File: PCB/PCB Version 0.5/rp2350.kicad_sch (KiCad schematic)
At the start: 27 parts, among them U1 RP2350A, U10 W25Q16JVUXIQ, Y1 Crystal_GND24

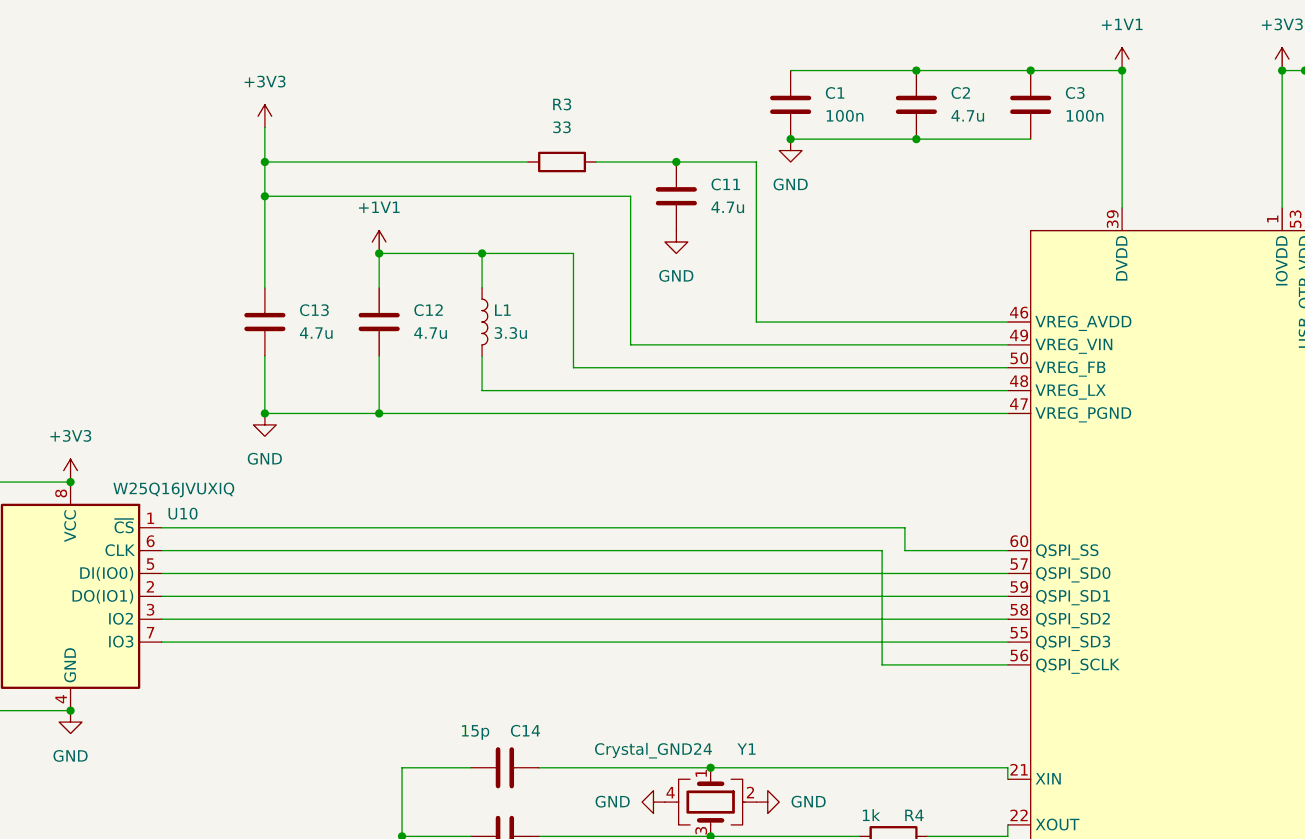
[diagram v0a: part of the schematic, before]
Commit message: add BOM
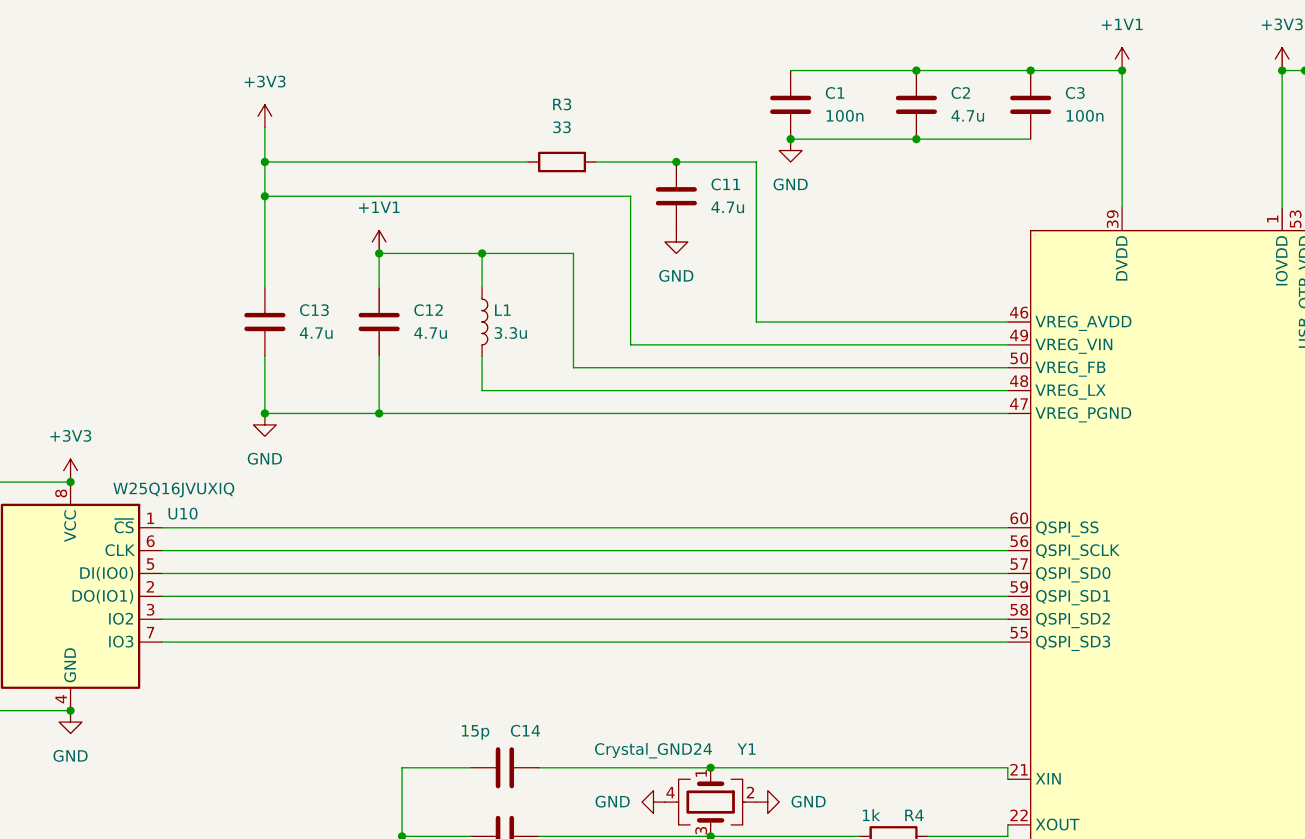
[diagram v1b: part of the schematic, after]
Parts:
- C11, C12, C13: footprint (none) -> Capacitor_SMD:C_0402_1005Metric
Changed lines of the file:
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@@
 	)
 	(junction
-		(at 100.33 92.71)
-		(diameter 0)
-		(color 0 0 0 0)
-	)
-	(junction
 		(at 278.13 82.55)
 		(diameter 0)
@@
 	)
 	(junction
+		(at 100.33 92.71)
+		(diameter 0)
+		(color 0 0 0 0)
+	)
+	(junction
 		(at 100.33 96.52)
 		(diameter 0)
@@
 	(wire
 		(pts
-			(xy 100.33 96.52) (xy 100.33 92.71)
-		)
-		(stroke
-			(width 0)
-			(type default)
-		)
-	)
-	(wire
-		(pts
 			(xy 240.03 234.95) (xy 240.03 246.38)
 		)
@@
 	(wire
 		(pts
-			(xy 168.91 135.89) (xy 168.91 148.59)
-		)
-		(stroke
-			(width 0)
-			(type default)
-		)
-	)
-	(wire
-		(pts
 			(xy 238.76 146.05) (xy 255.27 146.05)
 		)
@@
 	(wire
 		(pts
-			(xy 100.33 88.9) (xy 100.33 92.71)
+			(xy 238.76 171.45) (xy 255.27 171.45)
 		)
 		(stroke
@@
 	(wire
 		(pts
-			(xy 238.76 171.45) (xy 255.27 171.45)
+			(xy 238.76 153.67) (xy 255.27 153.67)
 		)
 		(stroke
@@
 		)
 	)
-	(wire
+	(bus
 		(pts
-			(xy 238.76 153.67) (xy 255.27 153.67)
+			(xy 257.81 166.37) (xy 257.81 168.91)
 		)
 		(stroke
@@
 		)
 	)
-	(bus
+	(wire
 		(pts
-			(xy 257.81 166.37) (xy 257.81 168.91)
+			(xy 100.33 88.9) (xy 100.33 92.71)
 		)
 		(stroke
@@
 	(wire
 		(pts
-			(xy 168.91 148.59) (xy 182.88 148.59)
-		)
-		(stroke
-			(width 0)
-			(type default)
-		)
-	)
-	(wire
-		(pts
 			(xy 238.76 176.53) (xy 255.27 176.53)
 		)
@@
 	(wire
 		(pts
-			(xy 88.9 135.89) (xy 168.91 135.89)
+			(xy 88.9 135.89) (xy 182.88 135.89)
 		)
 		(stroke
@@
 	(wire
 		(pts
-			(xy 88.9 133.35) (xy 171.45 133.35)
+			(xy 100.33 92.71) (xy 100.33 96.52)
+		)
+		(stroke
+			(width 0)
+			(type default)
+		)
+	)
+	(wire
+		(pts
+			(xy 88.9 133.35) (xy 182.88 133.35)
 		)
 		(stroke
@@
 	(wire
 		(pts
-			(xy 171.45 133.35) (xy 171.45 135.89)
-		)
-		(stroke
-			(width 0)
-			(type default)
-		)
-	)
-	(wire
-		(pts
 			(xy 48.26 153.67) (xy 60.96 153.67)
 		)
@@
 	(wire
 		(pts
-			(xy 171.45 135.89) (xy 182.88 135.89)
-		)
-		(stroke
-			(width 0)
-			(type default)
-		)
-	)
-	(wire
-		(pts
 			(xy 278.13 90.17) (xy 290.83 90.17)
 		)
@@
 			)
 		)
-		(property "Footprint" ""
+		(property "Footprint" "Capacitor_SMD:C_0402_1005Metric"
 			(at 147.0152 100.33 0)
 			(effects
@@
 			)
 		)
-		(property "Footprint" ""
+		(property "Footprint" "Capacitor_SMD:C_0402_1005Metric"
 			(at 113.9952 114.3 0)
 			(effects
@@
 			)
 		)
-		(property "Footprint" ""
+		(property "Footprint" "Capacitor_SMD:C_0402_1005Metric"
 			(at 101.2952 114.3 0)
 			(effects

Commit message: wip backup
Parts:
- removed C86: 100n, Capacitor_SMD:C_0402_1005Metric, symbol Device:C
- added SW1: ~, Kolibri custom:Button C530669, symbol Kolibri custom:SW_Push w/ GND
- C1, C10, C2, C3, C4, C5, C6, C7, C8, C9: footprint Capacitor_SMD:C_0402_1005Metric -> Capacitor_SMD:C_0402_1005Metric_Pad0.74x0.62mm_HandSolder
- L1: footprint (none) -> Kolibri custom:Abracon AOTA 0806
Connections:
- net GND: now also U10.9 (EP), SW1.2, SW1.3 (MP), SW1.4 (MP)
- net at U1.60 (QSPI_SS), U10.1 (~{CS}): now also SW1.1

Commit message: preliminary layout
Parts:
- C14, C15: footprint Capacitor_SMD:C_0402_1005Metric -> Capacitor_SMD:C_0402_1005Metric_Pad0.74x0.62mm_HandSolder
- R4, R7, R8: footprint Resistor_SMD:R_0402_1005Metric -> Resistor_SMD:R_0402_1005Metric_Pad0.72x0.64mm_HandSolder
- SW1: footprint Kolibri custom:Button C530669 -> Kolibri custom:Button C530669 wo holes
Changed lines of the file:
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@@
 (kicad_sch
-	(version 20231120)
+	(version 20250114)
 	(generator "eeschema")
-	(generator_version "8.0")
+	(generator_version "9.0")
 	(paper "A3")
 	(title_block
@@
 			)
 		)
-		(property "Footprint" "Resistor_SMD:R_0402_1005Metric"
+		(property "Footprint" "Resistor_SMD:R_0402_1005Metric_Pad0.72x0.64mm_HandSolder"
 			(at 170.18 169.418 90)
 			(effects
@@
 			)
 		)
-		(property "Footprint" "Capacitor_SMD:C_0402_1005Metric"
+		(property "Footprint" "Capacitor_SMD:C_0402_1005Metric_Pad0.74x0.62mm_HandSolder"
 			(at 130.81 166.6748 0)
 			(effects
@@
 			)
 		)
-		(property "Footprint" "Capacitor_SMD:C_0402_1005Metric"
+		(property "Footprint" "Capacitor_SMD:C_0402_1005Metric_Pad0.74x0.62mm_HandSolder"
 			(at 130.81 159.0548 0)
 			(effects
@@
 			)
 		)
-		(property "Footprint" "Resistor_SMD:R_0402_1005Metric"
+		(property "Footprint" "Resistor_SMD:R_0402_1005Metric_Pad0.72x0.64mm_HandSolder"
 			(at 238.252 231.14 90)
 			(effects
@@
 			)
 		)
-		(property "Footprint" "Resistor_SMD:R_0402_1005Metric"
+		(property "Footprint" "Resistor_SMD:R_0402_1005Metric_Pad0.72x0.64mm_HandSolder"
 			(at 248.412 231.14 90)
 			(effects
@@
 			)
 		)
-		(property "Footprint" "Kolibri custom:Button C530669"
+		(property "Footprint" "Kolibri custom:Button C530669 wo holes"
 			(at 105.41 175.768 0)
 			(effects

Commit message: wip routing
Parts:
- added R33: 1k, Resistor_SMD:R_0402_1005Metric_Pad0.72x0.64mm_HandSolder, symbol Device:R
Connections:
- net Motor.1: now also U1.35 (GPIO23); no longer U1.32 (GPIO20)
- net Motor.2: now also U1.34 (GPIO22); no longer U1.33 (GPIO21)
- net Motor.3: now also U1.33 (GPIO21); no longer U1.34 (GPIO22)
- net Motor.4: now also U1.32 (GPIO20); no longer U1.35 (GPIO23)
- net at U1.60 (QSPI_SS), U10.1 (~{CS}): now also R33.1; no longer SW1.1
- net SPI0.MOSI renamed SPI0.SDX
- new net: R33.2, SW1.1
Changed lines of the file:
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@@
+	)
+	(junction
+		(at 278.13 90.17)
+		(diameter 0)
+		(color 0 0 0 0)
+	)
+	(junction
+		(at 218.44 82.55)
+		(diameter 0)
+		(color 0 0 0 0)
+	)
+	(junction
+		(at 113.03 120.65)
+		(diameter 0)
+		(color 0 0 0 0)
+	)
+	(junction
+		(at 115.57 167.64)
+		(diameter 0)
+		(color 0 0 0 0)
+	)
+	(junction
+		(at 290.83 82.55)
+		(diameter 0)
+		(color 0 0 0 0)
+	)
+	(junction
+		(at 172.72 82.55)
+		(diameter 0)
+		(color 0 0 0 0)
+	)
+	(junction
+		(at 220.98 82.55)
+		(diameter 0)
+		(color 0 0 0 0)
+	)
+	(junction
+		(at 78.74 153.67)
+		(diameter 0)
+		(color 0 0 0 0)
+	)
+	(junction
+		(at 185.42 82.55)
+		(diameter 0)
+		(color 0 0 0 0)
 	)
 	(junction
@@
 	)
 	(junction
-		(at 278.13 90.17)
-		(diameter 0)
-		(color 0 0 0 0)
-	)
-	(junction
-		(at 218.44 82.55)
-		(diameter 0)
-		(color 0 0 0 0)
-	)
-	(junction
-		(at 113.03 120.65)
-		(diameter 0)
-		(color 0 0 0 0)
-	)
-	(junction
-		(at 115.57 167.64)
-		(diameter 0)
-		(color 0 0 0 0)
-	)
-	(junction
-		(at 290.83 82.55)
-		(diameter 0)
-		(color 0 0 0 0)
-	)
-	(junction
-		(at 172.72 82.55)
-		(diameter 0)
-		(color 0 0 0 0)
-	)
-	(junction
-		(at 220.98 82.55)
-		(diameter 0)
-		(color 0 0 0 0)
-	)
-	(junction
-		(at 78.74 153.67)
-		(diameter 0)
-		(color 0 0 0 0)
-	)
-	(junction
-		(at 185.42 82.55)
-		(diameter 0)
-		(color 0 0 0 0)
-	)
-	(junction
 		(at 252.73 90.17)
 		(diameter 0)
@@
 	(wire
 		(pts
+			(xy 97.79 133.35) (xy 182.88 133.35)
+		)
+		(stroke
+			(width 0)
+			(type default)
+		)
+	)
+	(wire
+		(pts
 			(xy 290.83 90.17) (xy 303.53 90.17)
 		)
@@
 	(wire
 		(pts
+			(xy 97.79 133.35) (xy 97.79 160.02)
+		)
+		(stroke
+			(width 0)
+			(type default)
+		)
+	)
+	(wire
+		(pts
 			(xy 123.19 160.02) (xy 115.57 160.02)
 		)
@@
 	(wire
 		(pts
-			(xy 97.79 133.35) (xy 182.88 133.35)
-		)
-		(stroke
-			(width 0)
-			(type default)
-		)
-	)
-	(wire
-		(pts
 			(xy 238.76 130.81) (xy 255.27 130.81)
 		)
@@
 		(pts
 			(xy 271.78 110.49) (xy 271.78 113.03)
-		)
-		(stroke
-			(width 0)
-			(type default)
-		)
-	)
-	(wire
-		(pts
-			(xy 97.79 133.35) (xy 97.79 167.64)
 		)
 		(stroke
@@
 		)
 	)
-	(label "Motor.2"
+	(label "Motor.3"
 		(at 255.27 171.45 180)
 		(effects
@@
 		)
 	)
-	(label "Motor.4"
+	(label "Motor.1"
 		(at 255.27 176.53 180)
 		(effects
@@
 		)
 	)
-	(label "Motor.1"
+	(label "Motor.4"
 		(at 255.27 168.91 180)
 		(effects
@@
 		)
 	)
-	(label "Motor.3"
+	(label "Motor.2"
 		(at 255.27 173.99 180)
 		(effects
@@
 		)
 	)
-	(label "SPI0.MOSI"
+	(label "SPI0.SDX"
 		(at 255.27 166.37 180)
 		(effects
@@
 					(unit 1)
 				)
+			)
+		)
+	)
+	(symbol
+		(lib_id "Device:R")
+		(at 97.79 163.83 0)
+		(unit 1)
+		(exclude_from_sim no)
+		(in_bom yes)
+		(on_board yes)
+		(dnp no)
+		(fields_autoplaced yes)
+		(property "Reference" "R33"
+			(at 100.33 162.5599 0)
+			(effects
+				(font
+					(size 1.27 1.27)
+				)
+				(justify left)
+			)
+		)
+		(property "Value" "1k"
+			(at 100.33 165.0999 0)
+			(effects
+				(font
+					(size 1.27 1.27)
+				)
+				(justify left)
+			)
+		)
+		(property "Footprint" "Resistor_SMD:R_0402_1005Metric_Pad0.72x0.64mm_HandSolder"
+			(at 96.012 163.83 90)
+			(effects
+				(font
+					(size 1.27 1.27)
+				)
+				(hide yes)
+			)
+		)
+		(property "Datasheet" "~"
+			(at 97.79 163.83 0)
+			(effects
+				(font
+					(size 1.27 1.27)
+				)
+				(hide yes)
+			)
+		)
+		(property "Description" "Resistor"
+			(at 97.79 163.83 0)
+			(effects
+				(font
+					(size 1.27 1.27)
+				)
+				(hide yes)
+			)
+		)
+		(pin "2"
+		)
+		(pin "1"
+		)
+		(instances
+			(project ""
+				(path "/1651f454-30c0-48ea-9fcf-6c96a661786a/68026f5c-72f7-45ff-bcb6-f836a66689ee"
+					(reference "R33")
+					(unit 1)
+				)

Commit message: finished routing
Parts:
- added R34, R35, R36, R37: 6.8k, Resistor_SMD:R_0402_1005Metric_Pad0.72x0.64mm_HandSolder, symbol Device:R
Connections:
- net +3V3: now also R34.1, R35.1, R36.1, R37.1
- net Motor.1: now also R34.2
- net Motor.2: now also R35.2
- net Motor.3: now also R36.2
- net Motor.4: now also R37.2
